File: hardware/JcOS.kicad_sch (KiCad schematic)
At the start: 6 parts, among them J1 Conn_01x04_Pin, J2 RPi_GPIO, SW1 SW_Push, U1 LCD-16X2

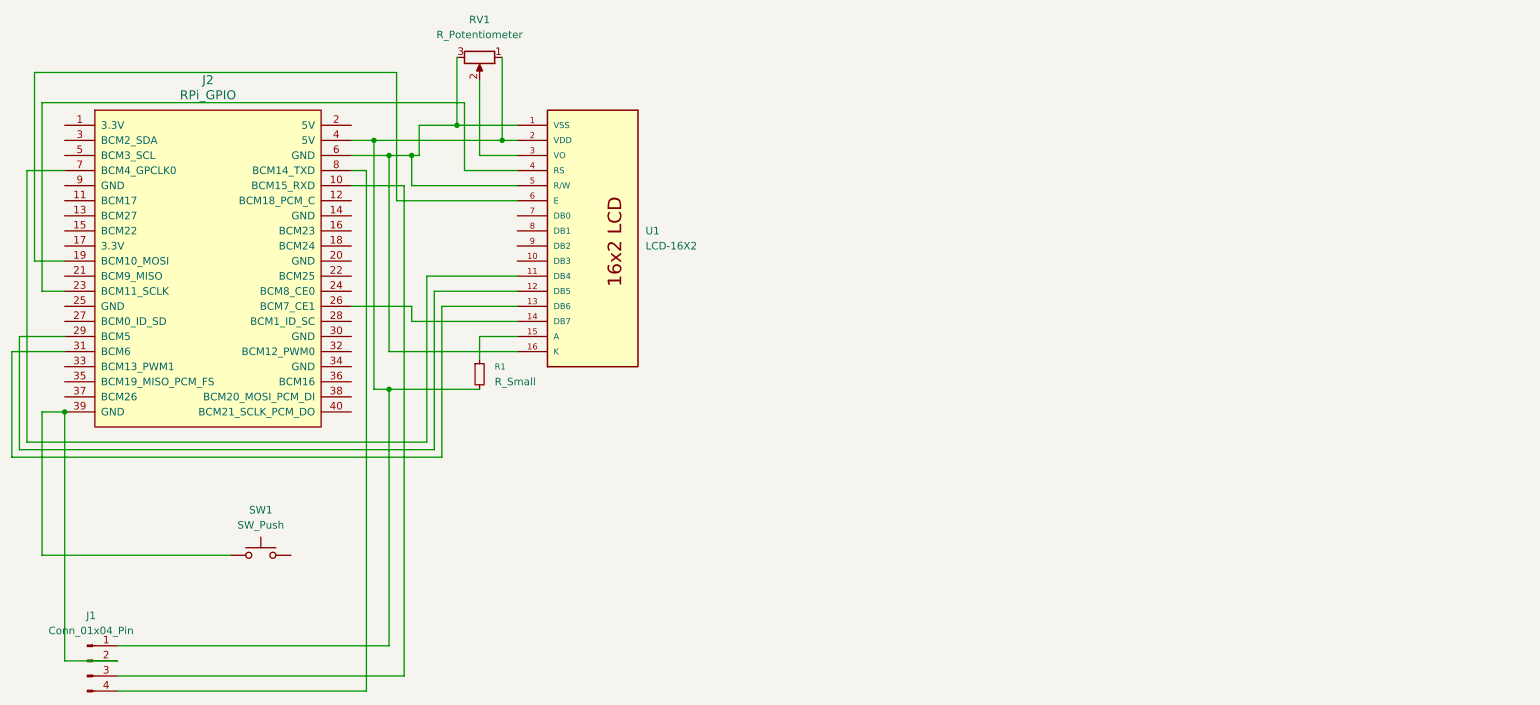
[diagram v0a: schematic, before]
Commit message: feat: 3.5" SPI TFT LCD hat board
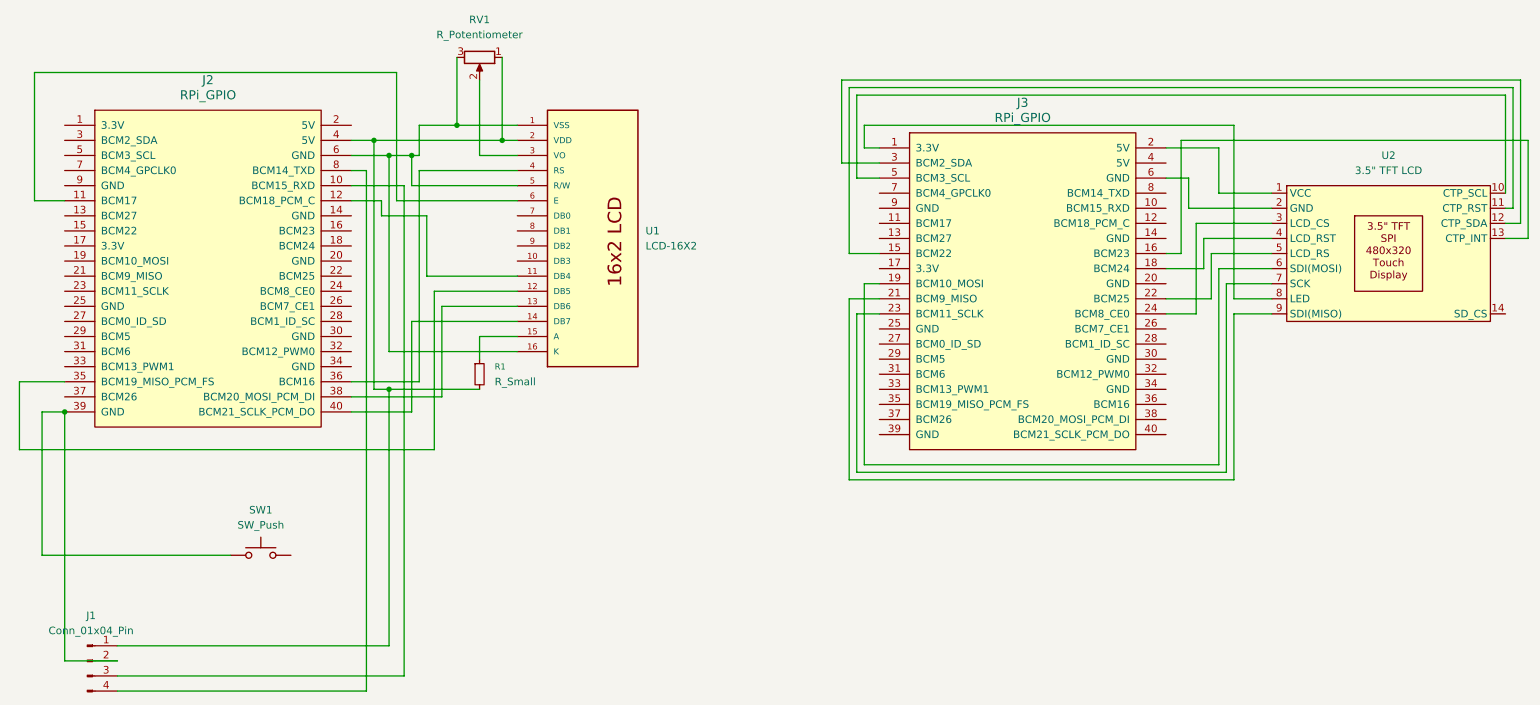
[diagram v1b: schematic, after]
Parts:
- added J3: RPi_GPIO, RPI_Hat:RPI_Hat_B+, symbol RPi_Hat:RPi_GPIO
- added U2: 3.5" TFT LCD, Display:3.5_ TFT LCD, symbol Display_Graphic:3.5{dblquote}_TFT_LCD
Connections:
- net at J2.11 (BCM17): now also U1.6 (E)
- net at J2.12 (BCM18_PCM_C): now also U1.11 (DB4)
- net at J2.19 (BCM10_MOSI): no longer U1.6 (E)
- net at J2.23 (BCM11_SCLK): no longer U1.4 (RS)
- net at J2.26 (BCM7_CE1): no longer U1.14 (DB7)
- net at J2.29 (BCM5): no longer U1.12 (DB5)
- net at J2.31 (BCM6): no longer U1.13 (DB6)
- net at J2.35 (BCM19_MISO_PCM_FS): now also U1.12 (DB5)
- net at J2.36 (BCM16): now also U1.4 (RS)
- net at J2.38 (BCM20_MOSI_PCM_DI): now also U1.13 (DB6)
- net at J2.40 (BCM21_SCLK_PCM_DO): now also U1.14 (DB7)
- net at J2.7 (BCM4_GPCLK0): no longer U1.11 (DB4)
- new net: J3.2 (5V), U2.1 (VCC)
- new net: J3.5 (BCM3_SCL), U2.10 (CTP_SCL)
- new net: J3.15 (BCM22), U2.11 (CTP_RST)
- new net: J3.3 (BCM2_SDA), U2.12 (CTP_SDA)
- new net: J3.16 (BCM23), U2.13 (CTP_INT)
- new net: J3.6 (GND), U2.2 (GND)
- new net: J3.24 (BCM8_CE0), U2.3 (LCD_CS)
- new net: J3.18 (BCM24), U2.4 (LCD_RST)
- new net: J3.22 (BCM25), U2.5 (LCD_RS)
- new net: J3.19 (BCM10_MOSI), U2.6 (SDI(MOSI))
- new net: J3.23 (BCM11_SCLK), U2.7 (SCK)
- new net: J3.1 (3.3V), U2.8 (LED)
- new net: J3.21 (BCM9_MISO), U2.9 (SDI(MISO))

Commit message: feat: reverse LCD PCB and add serial connector
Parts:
- added J4: Conn_01x04_Pin, Connector_PinHeader_2.54mm:PinHeader_1x04_P2.54mm_Vertical, symbol Connector:Conn_01x04_Pin
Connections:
- net at J3.22 (BCM25), U2.5 (LCD_RS): now also J3.8 (BCM14_TXD), J4.1 (Pin_1)
- net at J3.10 (BCM15_RXD): now also J4.2 (Pin_2)
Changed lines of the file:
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@@
 	(paper "A4")
+	(junction
+		(at 218.44 60.96)
+		(diameter 0)
+		(color 0 0 0 0)
+	)
+	(junction
+		(at 218.44 53.34)
+		(diameter 0)
+		(color 0 0 0 0)
+	)
 	(junction
 		(at 91.44 31.75)
@@
 	(wire
 		(pts
+			(xy 212.09 45.72) (xy 210.82 45.72)
+		)
+		(stroke
+			(width 0)
+			(type default)
+		)
+	)
+	(wire
+		(pts
 			(xy 217.17 50.8) (xy 217.17 55.88)
 		)
@@
 	(wire
 		(pts
+			(xy 218.44 53.34) (xy 218.44 60.96)
+		)
+		(stroke
+			(width 0)
+			(type default)
+		)
+	)
+	(wire
+		(pts
 			(xy 270.51 48.26) (xy 270.51 24.13)
 		)
@@
 	(wire
 		(pts
+			(xy 212.09 83.82) (xy 212.09 45.72)
+		)
+		(stroke
+			(width 0)
+			(type default)
+		)
+	)
+	(wire
+		(pts
 			(xy 220.98 58.42) (xy 220.98 90.17)
 		)
@@
 	(wire
 		(pts
-			(xy 218.44 53.34) (xy 218.44 60.96)
-		)
-		(stroke
-			(width 0)
-			(type default)
-		)
-	)
-	(wire
-		(pts
 			(xy 81.28 22.86) (xy 20.32 22.86)
 		)
@@
 	(wire
 		(pts
+			(xy 241.3 83.82) (xy 212.09 83.82)
+		)
+		(stroke
+			(width 0)
+			(type default)
+		)
+	)
+	(wire
+		(pts
 			(xy 219.71 43.18) (xy 219.71 35.56)
 		)
@@
 	(wire
 		(pts
+			(xy 218.44 60.96) (xy 218.44 81.28)
+		)
+		(stroke
+			(width 0)
+			(type default)
+		)
+	)
+	(wire
+		(pts
 			(xy 228.6 45.72) (xy 214.63 45.72)
 		)
@@
 	(wire
 		(pts
+			(xy 218.44 43.18) (xy 210.82 43.18)
+		)
+		(stroke
+			(width 0)
+			(type default)
+		)
+	)
+	(wire
+		(pts
 			(xy 219.71 35.56) (xy 210.82 35.56)
 		)
@@
 	(wire
 		(pts
+			(xy 218.44 43.18) (xy 218.44 53.34)
+		)
+		(stroke
+			(width 0)
+			(type default)
+		)
+	)
+	(wire
+		(pts
 			(xy 34.29 121.92) (xy 25.4 121.92)
 		)
@@
 		(pts
 			(xy 222.25 31.75) (xy 160.02 31.75)
+		)
+		(stroke
+			(width 0)
+			(type default)
+		)
+	)
+	(wire
+		(pts
+			(xy 241.3 81.28) (xy 218.44 81.28)
 		)
 		(stroke
@@
 					(unit 1)
 				)
+			)
+		)
+	)
+	(symbol
+		(lib_id "Connector:Conn_01x04_Pin")
+		(at 246.38 83.82 0)
+		(mirror y)
+		(unit 1)
+		(exclude_from_sim no)
+		(in_bom yes)
+		(on_board yes)
+		(dnp no)
+		(property "Reference" "J4"
+			(at 245.745 76.2 0)
+			(effects
+				(font
+					(size 1.27 1.27)
+				)
+			)
+		)
+		(property "Value" "Conn_01x04_Pin"
+			(at 246.126 78.486 0)
+			(effects
+				(font
+					(size 1.27 1.27)
+				)
+			)
+		)
+		(property "Footprint" "Connector_PinHeader_2.54mm:PinHeader_1x04_P2.54mm_Vertical"
+			(at 246.38 83.82 0)
+			(effects
+				(font
+					(size 1.27 1.27)
+				)
+				(hide yes)
+			)
+		)
+		(property "Datasheet" "~"
+			(at 246.38 83.82 0)
+			(effects
+				(font
+					(size 1.27 1.27)
+				)
+				(hide yes)
+			)
+		)
+		(property "Description" "Generic connector, single row, 01x04, script generated"
+			(at 246.38 83.82 0)
+			(effects
+				(font
+					(size 1.27 1.27)
+				)
+				(hide yes)
+			)
+		)
+		(pin "2"
+		)
+		(pin "3"
+		)
+		(pin "4"
+		)
+		(pin "1"
+		)
+		(instances
+			(project "JcOS"
+				(path "/da952d82-aa68-4938-b135-3f671031b6b5"
+					(reference "J4")
+					(unit 1)
+				)

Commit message: feat: wire up tft spi lcd
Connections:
- net at J3.22 (BCM25), U2.5 (LCD_RS): no longer J3.8 (BCM14_TXD), J4.1 (Pin_1)
- net at J4.2 (Pin_2): no longer J3.10 (BCM15_RXD)
- net at J4.3 (Pin_3): now also J3.8 (BCM14_TXD)
- net at J4.4 (Pin_4): now also J3.10 (BCM15_RXD)
- net at J3.14 (GND): now also J4.1 (Pin_1)
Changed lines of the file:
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@@
 	(paper "A4")
-	(junction
-		(at 218.44 60.96)
-		(diameter 0)
-		(color 0 0 0 0)
-	)
-	(junction
-		(at 218.44 53.34)
-		(diameter 0)
-		(color 0 0 0 0)
-	)
 	(junction
 		(at 91.44 31.75)
@@
 	(wire
 		(pts
+			(xy 227.33 57.15) (xy 227.33 53.34)
+		)
+		(stroke
+			(width 0)
+			(type default)
+		)
+	)
+	(wire
+		(pts
 			(xy 271.78 50.8) (xy 271.78 34.29)
 		)
@@
 	(wire
 		(pts
+			(xy 224.79 81.28) (xy 224.79 49.53)
+		)
+		(stroke
+			(width 0)
+			(type default)
+		)
+	)
+	(wire
+		(pts
 			(xy 269.24 45.72) (xy 269.24 25.4)
 		)
@@
 	(wire
 		(pts
+			(xy 227.33 53.34) (xy 228.6 53.34)
+		)
+		(stroke
+			(width 0)
+			(type default)
+		)
+	)
+	(wire
+		(pts
 			(xy 101.6 69.85) (xy 80.01 69.85)
 		)
@@
 	(wire
 		(pts
-			(xy 218.44 53.34) (xy 218.44 60.96)
+			(xy 218.44 43.18) (xy 218.44 86.36)
 		)
 		(stroke
@@
 	(wire
 		(pts
+			(xy 241.3 81.28) (xy 224.79 81.28)
+		)
+		(stroke
+			(width 0)
+			(type default)
+		)
+	)
+	(wire
+		(pts
 			(xy 215.9 63.5) (xy 210.82 63.5)
 		)
@@
 	(wire
 		(pts
-			(xy 212.09 83.82) (xy 212.09 45.72)
+			(xy 212.09 45.72) (xy 212.09 93.98)
 		)
 		(stroke
@@
 	(wire
 		(pts
+			(xy 224.79 49.53) (xy 214.63 49.53)
+		)
+		(stroke
+			(width 0)
+			(type default)
+		)
+	)
+	(wire
+		(pts
 			(xy 81.28 22.86) (xy 20.32 22.86)
 		)
@@
 	(wire
 		(pts
+			(xy 217.17 57.15) (xy 227.33 57.15)
+		)
+		(stroke
+			(width 0)
+			(type default)
+		)
+	)
+	(wire
+		(pts
 			(xy 156.21 24.13) (xy 156.21 38.1)
 		)
@@
 	(wire
 		(pts
+			(xy 212.09 93.98) (xy 231.14 93.98)
+		)
+		(stroke
+			(width 0)
+			(type default)
+		)
+	)
+	(wire
+		(pts
 			(xy 95.25 76.2) (xy 80.01 76.2)
 		)
@@
 	(wire
 		(pts
+			(xy 210.82 60.96) (xy 217.17 60.96)
+		)
+		(stroke
+			(width 0)
+			(type default)
+		)
+	)
+	(wire
+		(pts
 			(xy 228.6 50.8) (xy 217.17 50.8)
 		)
@@
 	(wire
 		(pts
+			(xy 217.17 60.96) (xy 217.17 57.15)
+		)
+		(stroke
+			(width 0)
+			(type default)
+		)
+	)
+	(wire
+		(pts
 			(xy 267.97 45.72) (xy 269.24 45.72)
 		)
@@
 	(wire
 		(pts
-			(xy 241.3 83.82) (xy 212.09 83.82)
-		)
-		(stroke
-			(width 0)
-			(type default)
-		)
-	)
-	(wire
-		(pts
 			(xy 219.71 43.18) (xy 219.71 35.56)
 		)
@@
 	(wire
 		(pts
-			(xy 218.44 60.96) (xy 218.44 81.28)
-		)
-		(stroke
-			(width 0)
-			(type default)
-		)
-	)
-	(wire
-		(pts
 			(xy 228.6 45.72) (xy 214.63 45.72)
 		)
@@
 	(wire
 		(pts
+			(xy 231.14 93.98) (xy 231.14 88.9)
+		)
+		(stroke
+			(width 0)
+			(type default)
+		)
+	)
+	(wire
+		(pts
 			(xy 77.47 34.29) (xy 73.66 34.29)
 		)
@@
 	(wire
 		(pts
-			(xy 214.63 40.64) (xy 210.82 40.64)
+			(xy 210.82 40.64) (xy 214.63 40.64)
 		)
 		(stroke
@@
 	(wire
 		(pts
+			(xy 231.14 88.9) (xy 241.3 88.9)
+		)
+		(stroke
+			(width 0)
+			(type default)
+		)
+	)
+	(wire
+		(pts
 			(xy 20.32 44.45) (xy 25.4 44.45)
 		)
@@
 	(wire
 		(pts
-			(xy 218.44 43.18) (xy 218.44 53.34)
-		)
-		(stroke
-			(width 0)
-			(type default)
-		)
-	)
-	(wire
-		(pts
 			(xy 34.29 121.92) (xy 25.4 121.92)
 		)
@@
 	(wire
 		(pts
-			(xy 218.44 60.96) (xy 210.82 60.96)
-		)
-		(stroke
-			(width 0)
-			(type default)
-		)
-	)
-	(wire
-		(pts
 			(xy 99.06 20.32) (xy 99.06 34.29)
 		)
@@
 	(wire
 		(pts
-			(xy 228.6 53.34) (xy 218.44 53.34)
-		)
-		(stroke
-			(width 0)
-			(type default)
-		)
-	)
-	(wire
-		(pts
 			(xy 85.09 39.37) (xy 85.09 74.93)
 		)
@@
 	(wire
 		(pts
-			(xy 241.3 81.28) (xy 218.44 81.28)
+			(xy 214.63 49.53) (xy 214.63 50.8)
 		)
 		(stroke
@@
 	(wire
 		(pts
+			(xy 214.63 50.8) (xy 210.82 50.8)
+		)
+		(stroke
+			(width 0)
+			(type default)
+		)
+	)
+	(wire
+		(pts
 			(xy 270.51 24.13) (xy 156.21 24.13)
 		)
@@
 		)
 		(stroke
+			(width 0)
+			(type default)
+		)
+	)
+	(wire
+		(pts
+			(xy 218.44 86.36) (xy 241.3 86.36)
+		)
+		(stroke
